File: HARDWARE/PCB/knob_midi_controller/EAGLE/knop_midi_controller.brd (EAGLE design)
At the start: 99.9 x 99.9 mm, 26 parts

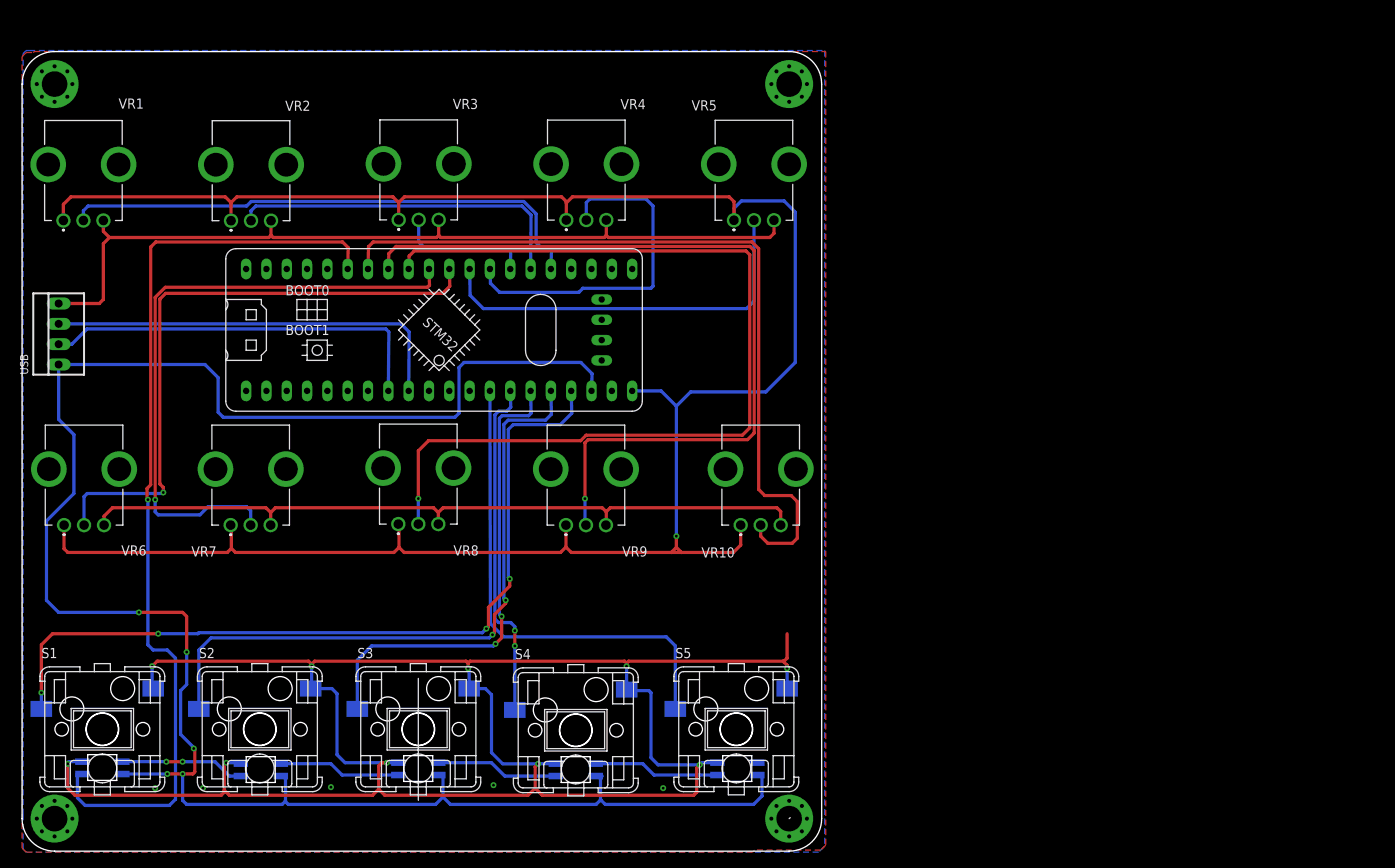
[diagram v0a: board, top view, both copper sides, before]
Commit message: FEAT: fix problem placement pcb and add name and logo
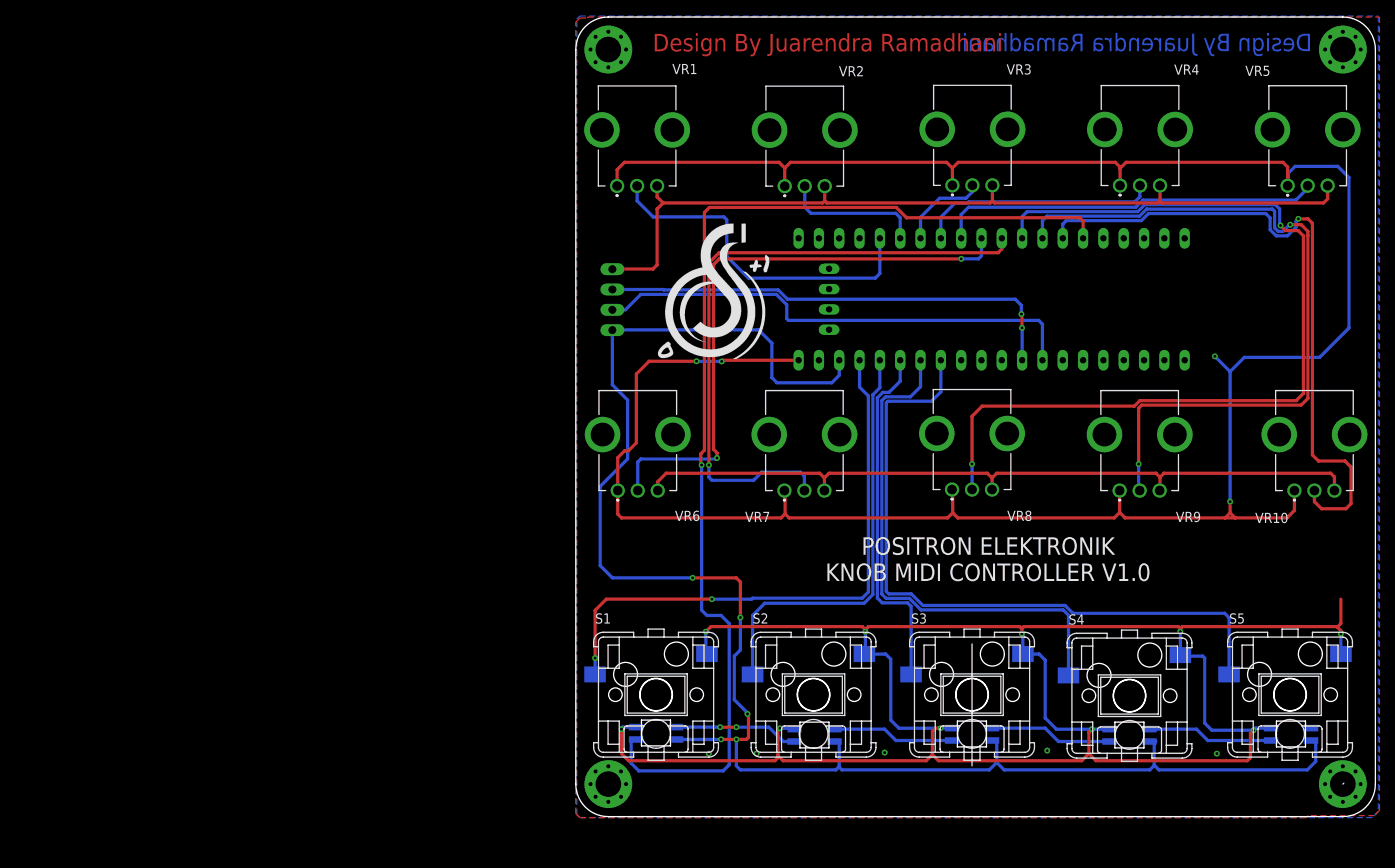
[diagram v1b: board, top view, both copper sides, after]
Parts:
- moved MOD1 86.9 mm to (130.1, 62.6), flipped to the bottom
- moved VR10 69.3 mm to (161.5, 44.3)
- moved H1 69.3 mm to (73.3, 2.03)
- moved H3 69.3 mm to (73.3, 93.9)
- moved LED1 69.3 mm to (79.2, 8.38)
- moved LED2 69.3 mm to (99.1, 8.13)
- moved LED3 69.3 mm to (118.7, 8.26)
- moved LED4 69.3 mm to (138.4, 8.13)
- moved S1 69.3 mm to (79.2, 13.2)
- moved S2 69.3 mm to (98.9, 13.2)
- moved S3 69.3 mm to (118.7, 13.2)
- moved S4 69.3 mm to (138.4, 13.1)
- moved S5 69.3 mm to (158.5, 13.2)
- moved VR3 69.3 mm to (118.8, 82.5)
- moved VR4 69.3 mm to (139.7, 82.5)
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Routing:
- net +5V/1: track 253.1 -> 208.1 mm
- net +3V3: track 269.8 -> 303.0 mm, vias 1 -> 4
- net BUT1: track 102.2 -> 72.6 mm, vias 4 -> 2
- net BUT2: track 81.3 -> 53.1 mm, vias 2 -> 0
- net POT2: track 43.7 -> 17.7 mm
- net BUT5: track 61.2 -> 86.2 mm
- net POT1: track 67.1 -> 43.5 mm
- net RGB: track 116.2 -> 138.7 mm
- net BUT4: track 43.2 -> 65.0 mm, vias 2 -> 0
- net POT10: track 98.9 -> 82.7 mm, vias 0 -> 1
- net BUT3: track 59.9 -> 44.5 mm, vias 2 -> 0
- net POT4: track 44.0 -> 30.0 mm
- net D-: track 49.6 -> 61.6 mm
- net POT9: track 103.0 -> 91.9 mm, vias 1 -> 2
- net D+: track 51.6 -> 59.2 mm, vias 0 -> 2
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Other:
- board text added: "Design By Juarendra Ramadhani"
- board text added: "POSITRON ELEKTRONIK KNOB MIDI CONTROLLER V1.0"
